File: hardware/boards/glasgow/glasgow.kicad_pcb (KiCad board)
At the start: 4 copper layers, 80 x 49 mm, 121 parts, among them J1 USB_B_Micro, J2 Conn_02x10_Odd_Even, J3 Conn_02x10_Odd_Even, J4 Conn_01x02, U1 CY7C68013A-56LTX, U10 DAC081C081CIMK, U11 TPS73101DBV, U12 ADC081C021CIMM, U13 DAC081C081CIMK, U14 TPS73101DBV, U2 CAT24M01W, U3 CAT24C256W, U4 ICE40UP5K-SG48ITR, U5 FXMA108BQX, U6 FXMA108BQX, U7 LM3880MF-1AF, U8 MIC5355-S4YMME, U9 ADC081C021CIMM, Y1 24M

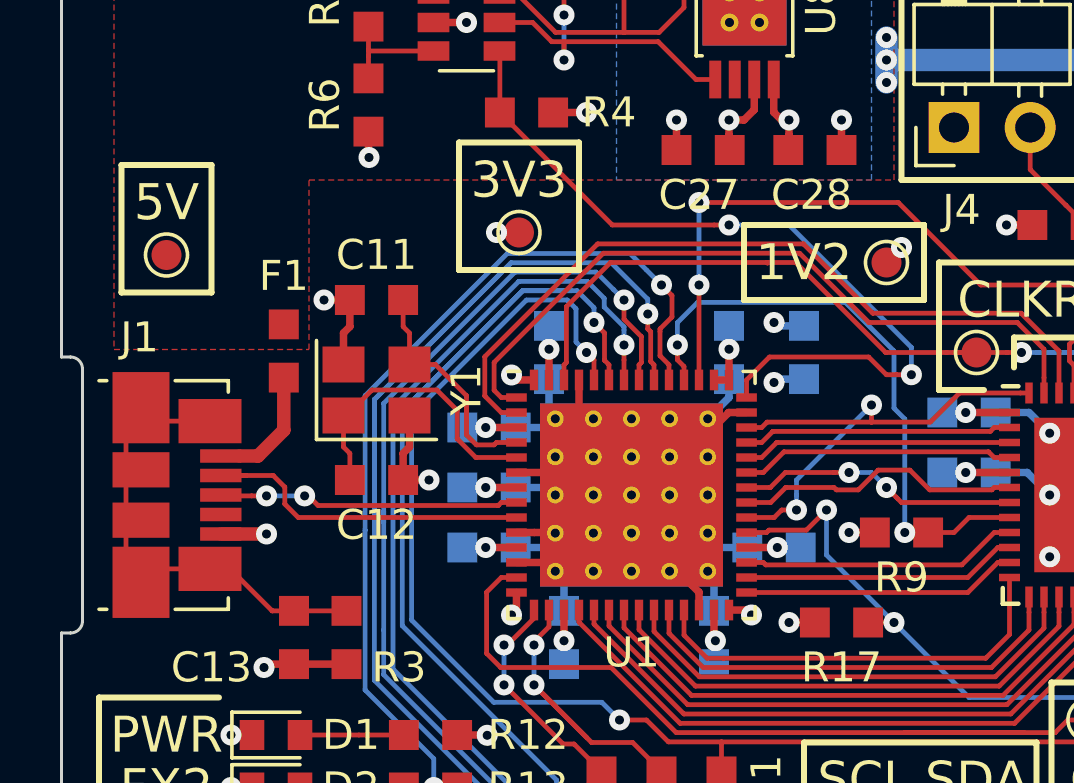
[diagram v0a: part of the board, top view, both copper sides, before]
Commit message: Add USB protection IC.
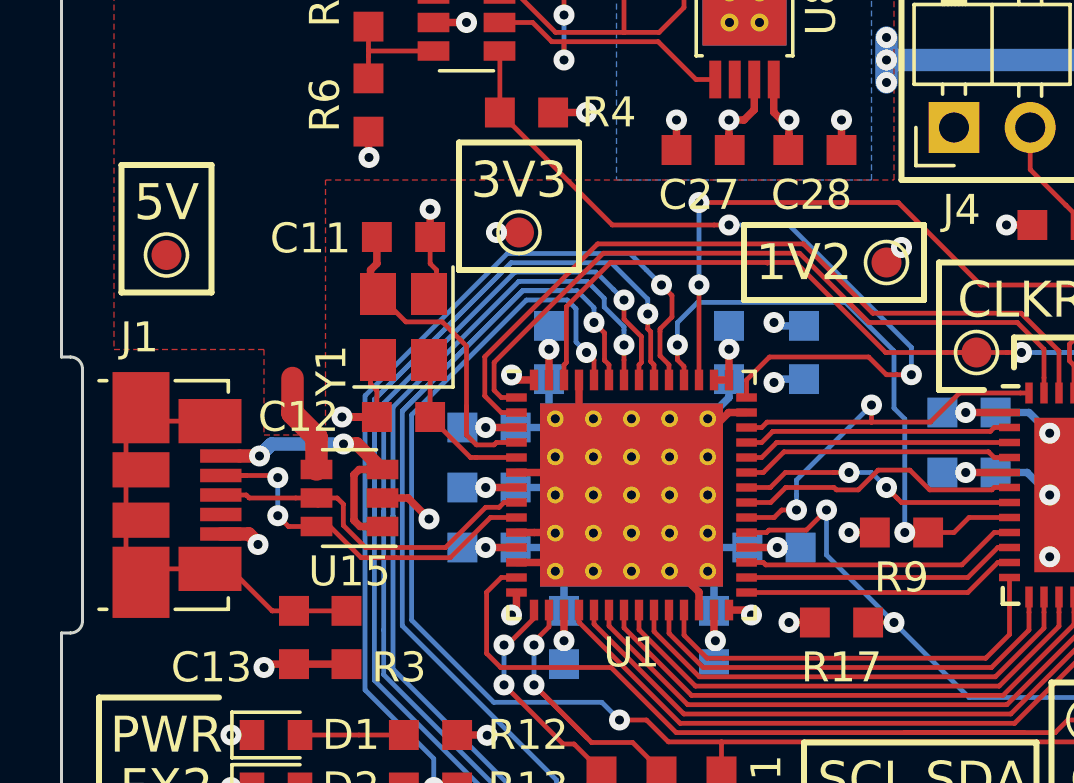
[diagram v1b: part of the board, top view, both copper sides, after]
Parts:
- removed F1: 500m, Fuse:Fuse_0603_1608Metric_Pad0.99x1.00mm_HandSolder
- added U15: TPD3S014, TO_SOT_Packages_SMD:SOT-23-6, F.Cu at (59.6, 95.6)
- moved C11 2.28 mm to (61.4, 86.9), turned to 0 degrees
- moved C12 2.28 mm to (61.4, 92.9), turned to 180 degrees
- moved Y1 2.28 mm to (61.4, 89.9), turned to 90 degrees
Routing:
- net /VUSB: track 3.57 -> 9.29 mm, vias 0 -> 2
- net /XTALIN: track 9.84 -> 5.90 mm
- net +5V: track 81.9 -> 85.3 mm
- net GND: track 112.0 -> 115.3 mm, vias 55 -> 56
- net /XTALOUT: track 8.35 -> 11.5 mm
- net /USB_N: track 12.0 -> 14.8 mm, vias 0 -> 2
- net /USB_P: track 9.89 -> 12.2 mm, vias 2 -> 0
